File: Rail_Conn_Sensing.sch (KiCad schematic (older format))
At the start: 35 parts, among them U1 AMC1200, U2 AMC1200

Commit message: Upload version 2 files with footprints
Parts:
- removed BT? (x2): 9V, symbol Device:Battery
- removed C? (x2): 100uF, symbol Device:C
- removed D? (x2): Zener, symbol Device:D_Zener
- removed J?: Output, symbol Connector:Screw_Terminal_01x01
- removed R? (x2): 220, symbol Device:R
- added C1, C2, C3, C4: 10uF, symbol Device:C
- added D1, D2: GREEN, symbol Device:LED
- added J3: Outputs, symbol Connector:Screw_Terminal_01x03
- added PS1, PS2: PQMCE1-S5-S5-S, Rail_Conn_Sensing-footprints:CONV_PQMCE1-S5-S5-S, symbol PQMCE1-S5-S5-S:PQMCE1-S5-S5-S
- added R10, R9: 100, Resistor_THT:R_Axial_DIN0207_L6.3mm_D2.5mm_P10.16mm_Horizontal, symbol Device:R
- added unit 4 of U4
- added unit 3 of U4
- R1, R11, R2, R3, R4: renamed from R?; footprint (none) -> Resistor_THT:R_Axial_DIN0207_L6.3mm_D2.5mm_P10.16mm_Horizontal
- R5, R7: renamed from R?; value 10k -> 600; footprint (none) -> Resistor_THT:R_Axial_DIN0207_L6.3mm_D2.5mm_P10.16mm_Horizontal
- R6, R8: renamed from R?; value 1k -> 400; footprint (none) -> Resistor_THT:R_Axial_DIN0207_L6.3mm_D2.5mm_P10.16mm_Horizontal
- U1, U2: footprint (none) -> Rail_Conn_Sensing-footprints:SOIC-8_W7.6mm
- gave numbers to parts that had none: 7
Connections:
- net +3V3 is gone; now on net +5V: U1.8 (VDD2), U2.8 (VDD2)
- net +5V: now also R11.2, U5.5, C4.1, PS1.1 (VIN), PS2.1 (VIN), R10.2, R9.2; no longer R11.1, U5.4
- net GND: now also C3.2, C4.2, PS1.2 (GND), PS2.2 (GND)
- net at J1.2 (Pin_2), R3.2, U1.3 (VINN)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: now also C1.2, PS2.4 (0V)
- net at U1.1 (VDD1): now also C1.1, PS2.6 (+VO)
- net at U2.1 (VDD1): now also C2.1, PS1.6 (+VO)
- net at J1.4 (Pin_4), R4.2, U2.3 (VINN)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: now also C2.2, PS1.4 (0V)
- net at U4.3, U5.1: now also U4.9
- net at U4.6, U5.2: now also U4.13
- net at U5.3: now also U5.4, U4.10, U4.12; no longer U5.5
- net at D3.1 (K), U5.6: now also J3.2 (Pin_2)
- net at D3.2 (A): now also R11.1; no longer R11.2
- net at J2.1 (Pin_1), U6.1 (IN): now also C3.1
- new net: D2.1 (K), J3.3 (Pin_3), U4.11
- new net: D1.1 (K), J3.1 (Pin_1), U4.8
- new net: D1.2 (A), R9.1
- new net: D2.2 (A), R10.1
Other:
- moved on the sheet: D3, J1, J2, R1, R11, R2, R3, R4, R5, R6, R7, R8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

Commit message: Create pcb layout and part assignment
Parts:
- C1, C2, C3, C4: footprint (none) -> Capacitor_THT:C_Radial_D6.3mm_H11.0mm_P2.50mm
- D1, D2, D3: footprint (none) -> LED_THT:LED_D5.0mm
- J1: footprint (none) -> TerminalBlock_Phoenix:TerminalBlock_Phoenix_PT-1,5-4-5.0-H_1x04_P5.00mm_Horizontal
- J2: footprint (none) -> TerminalBlock_Phoenix:TerminalBlock_Phoenix_PT-1,5-2-5.0-H_1x02_P5.00mm_Horizontal
- J3: footprint (none) -> TerminalBlock_Phoenix:TerminalBlock_Phoenix_PT-1,5-3-5.0-H_1x03_P5.00mm_Horizontal
- R1, R10, R11, R2, R3, R4, R5, R6, R7, R8, R9: footprint Resistor_THT:R_Axial_DIN0207_L6.3mm_D2.5mm_P10.16mm_Horizontal -> Resistor_THT:R_Axial_DIN0309_L9.0mm_D3.2mm_P15.24mm_Horizontal
- U3, U4, U5: footprint (none) -> Package_DIP:DIP-14_W7.62mm
- U6: footprint (none) -> Package_TO_SOT_THT:TO-220-3_Horizontal_TabDown

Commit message: Delete extra resistor divider and re-arrange pcb
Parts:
- removed R7: 600, Resistor_THT:R_Axial_DIN0309_L9.0mm_D3.2mm_P15.24mm_Horizontal, symbol Device:R
- removed R8: 400, Resistor_THT:R_Axial_DIN0309_L9.0mm_D3.2mm_P15.24mm_Horizontal, symbol Device:R
- renumbered R9 to R7, R10 to R8, R11 to R9
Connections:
- net at R5.2, R6.1, U3.2 (-)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: now also U3.13 (-), U3.9 (-)
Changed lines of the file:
@@
 Sheet 1 1
 Title "Rail Connection Sensing Circuit"
-Date "2020-06-26"
+Date "2020-06-30"
 Rev "v02"
 Comp ""
@@
 $EndComp
 $Comp
-L power:GND #PWR07
+L power:GND #PWR08
 U 1 1 5EE5082A
 P 4800 3800
-F 0 "#PWR07" H 4800 3550 50  0001 C CNN
+F 0 "#PWR08" H 4800 3550 50  0001 C CNN
 F 1 "GND" H 4805 3627 50  0000 C CNN
 F 2 "" H 4800 3800 50  0001 C CNN
@@
 Wire Wire Line
 	5300 5400 4650 5400
-$Comp
-L Device:R R7
-U 1 1 5EEC90AA
-P 4800 4800
-F 0 "R7" H 4870 4846 50  0000 L CNN
-F 1 "600" H 4870 4755 50  0000 L CNN
-F 2 "Resistor_THT:R_Axial_DIN0309_L9.0mm_D3.2mm_P15.24mm_Horizontal" V 4730 4800 50  0001 C CNN
-F 3 "~" H 4800 4800 50  0001 C CNN
-	1    4800 4800
-	1    0    0    -1
-$EndComp
-$Comp
-L Device:R R8
-U 1 1 5EEC90B0
-P 4800 5200
-F 0 "R8" H 4870 5246 50  0000 L CNN
-F 1 "400" H 4870 5155 50  0000 L CNN
-F 2 "Resistor_THT:R_Axial_DIN0309_L9.0mm_D3.2mm_P15.24mm_Horizontal" V 4730 5200 50  0001 C CNN
-F 3 "~" H 4800 5200 50  0001 C CNN
-	1    4800 5200
-	1    0    0    -1
-$EndComp
 Wire Wire Line
 	4650 5200 4650 5400
@@
 $EndComp
 Wire Wire Line
-	4800 4950 4800 5000
-Wire Wire Line
-	5100 4800 5100 5000
-Wire Wire Line
-	5100 5000 4800 5000
-Connection ~ 4800 5000
-Wire Wire Line
-	4800 5000 4800 5050
-Wire Wire Line
 	5300 5600 5100 5600
 Wire Wire Line
-	5100 5600 5100 5000
-Connection ~ 5100 5000
-Wire Wire Line
 	4450 5200 4650 5200
 Wire Wire Line
 	4450 5300 4550 5300
-Wire Wire Line
-	4550 5300 4550 5500
-Wire Wire Line
-	4800 5350 4800 5500
-Wire Wire Line
-	4550 5500 4800 5500
 $Comp
 L Device:LED D3
@@
 	1    0    0    -1
 $EndComp
-Connection ~ 4800 5500
-$Comp
-L power:GND #PWR08
+$Comp
+L power:GND #PWR03
 U 1 1 5EEC90BD
-P 4800 5550
-F 0 "#PWR08" H 4800 5300 50  0001 C CNN
-F 1 "GND" H 4805 5377 50  0000 C CNN
-F 2 "" H 4800 5550 50  0001 C CNN
-F 3 "" H 4800 5550 50  0001 C CNN
-	1    4800 5550
-	1    0    0    -1
-$EndComp
-Wire Wire Line
-	4800 5500 4800 5550
+P 4550 5550
+F 0 "#PWR03" H 4550 5300 50  0001 C CNN
+F 1 "GND" H 4555 5377 50  0000 C CNN
+F 2 "" H 4550 5550 50  0001 C CNN
+F 3 "" H 4550 5550 50  0001 C CNN
+	1    4550 5550
+	1    0    0    -1
+$EndComp
 Wire Wire Line
 	4800 3500 4800 3800
@@
 	2400 5300 2800 5300
 $Comp
-L Device:R R11
+L Device:R R9
 U 1 1 5F029A20
 P 9200 3650
-F 0 "R11" H 9270 3696 50  0000 L CNN
+F 0 "R9" H 9270 3696 50  0000 L CNN
 F 1 "100" H 9270 3605 50  0000 L CNN
 F 2 "Resistor_THT:R_Axial_DIN0309_L9.0mm_D3.2mm_P15.24mm_Horizontal" V 9130 3650 50  0001 C CNN
@@
 $EndComp
 $Comp
-L power:+5V #PWR05
+L power:+5V #PWR06
 U 1 1 5EEB13E3
 P 4700 1300
-F 0 "#PWR05" H 4700 1150 50  0001 C CNN
+F 0 "#PWR06" H 4700 1150 50  0001 C CNN
 F 1 "+5V" H 4715 1473 50  0000 C CNN
 F 2 "" H 4700 1300 50  0001 C CNN
@@
 	4550 2500 4550 2400
 Wire Wire Line
-	4550 4400 4550 4450
-Wire Wire Line
-	4800 4650 4800 4450
-Wire Wire Line
-	4800 4450 4550 4450
-Connection ~ 4550 4450
-Wire Wire Line
-	4550 4450 4550 5000
-Wire Wire Line
 	3450 3200 3650 3200
 Wire Wire Line
@@
 $EndComp
 $Comp
-L Device:R R10
+L Device:R R8
 U 1 1 5F0A91A6
 P 8600 4650
-F 0 "R10" H 8670 4696 50  0000 L CNN
+F 0 "R8" H 8670 4696 50  0000 L CNN
 F 1 "100" H 8670 4605 50  0000 L CNN
 F 2 "Resistor_THT:R_Axial_DIN0309_L9.0mm_D3.2mm_P15.24mm_Horizontal" V 8530 4650 50  0001 C CNN
@@
 	8800 3550 8750 3550
 $Comp
-L Device:R R9
+L Device:R R7
 U 1 1 5F094ED0
 P 8600 3550
-F 0 "R9" H 8670 3596 50  0000 L CNN
+F 0 "R7" H 8670 3596 50  0000 L CNN
 F 1 "100" H 8670 3505 50  0000 L CNN
 F 2 "Resistor_THT:R_Axial_DIN0309_L9.0mm_D3.2mm_P15.24mm_Horizontal" V 8530 3550 50  0001 C CNN
@@
 	4500 1600 4700 1600
 $Comp
-L power:GND #PWR06
+L power:GND #PWR07
 U 1 1 5EEB771F
 P 4700 1650
-F 0 "#PWR06" H 4700 1400 50  0001 C CNN
+F 0 "#PWR07" H 4700 1400 50  0001 C CNN
 F 1 "GND" H 4705 1477 50  0000 C CNN
 F 2 "" H 4700 1650 50  0001 C CNN
@@
 	4500 1400 4700 1400
 $Comp
-L power:+5V #PWR03
+L power:+5V #PWR04
 U 1 1 5F386CEF
 P 4650 6200
-F 0 "#PWR03" H 4650 6050 50  0001 C CNN
+F 0 "#PWR04" H 4650 6050 50  0001 C CNN
 F 1 "+5V" H 4665 6373 50  0000 C CNN
 F 2 "" H 4650 6200 50  0001 C CNN
@@
 	4450 6500 4650 6500
 $Comp
-L power:GND #PWR04
+L power:GND #PWR05
 U 1 1 5F386CF7
 P 4650 6550
-F 0 "#PWR04" H 4650 6300 50  0001 C CNN
+F 0 "#PWR05" H 4650 6300 50  0001 C CNN
 F 1 "GND" H 4655 6377 50  0000 C CNN
 F 2 "" H 4650 6550 50  0001 C CNN
@@
 	2100 6200 2100 4850
 Connection ~ 3250 6200
+Wire Wire Line
+	4550 4400 4550 5000
+Wire Wire Line
+	5100 4800 5100 5600
+Wire Wire Line
+	4550 5300 4550 5550
+Wire Wire Line
+	5100 4800 5100 3600
+Connection ~ 5100 4800
+Connection ~ 5100 3600
 $EndSCHEMATC

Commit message: Fix up wires and move silk screen labels
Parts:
- C1, C2, C3, C4: footprint Capacitor_THT:C_Radial_D6.3mm_H11.0mm_P2.50mm -> Capacitor_THT:CP_Radial_D6.3mm_P2.50mm; symbol Device:C -> Device:CP1
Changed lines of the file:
@@
 	4450 6300 4650 6300
 $Comp
-L Device:C C1
+L Device:CP1 C1
 U 1 1 5EF2E610
 P 3150 1550
 F 0 "C1" H 3265 1596 50  0000 L CNN
 F 1 "10uF" H 3265 1505 50  0000 L CNN
-F 2 "Capacitor_THT:C_Radial_D6.3mm_H11.0mm_P2.50mm" H 3188 1400 50  0001 C CNN
+F 2 "Capacitor_THT:CP_Radial_D6.3mm_P2.50mm" H 3188 1400 50  0001 C CNN
 F 3 "~" H 3150 1550 50  0001 C CNN
 	1    3150 1550
@@
 	2050 1700 2050 3450
 $Comp
-L Device:C C3
+L Device:CP1 C3
 U 1 1 5EF511EA
 P 7050 1750
 F 0 "C3" H 7165 1796 50  0000 L CNN
 F 1 "10uF" H 7165 1705 50  0000 L CNN
-F 2 "Capacitor_THT:C_Radial_D6.3mm_H11.0mm_P2.50mm" H 7088 1600 50  0001 C CNN
+F 2 "Capacitor_THT:CP_Radial_D6.3mm_P2.50mm" H 7088 1600 50  0001 C CNN
 F 3 "~" H 7050 1750 50  0001 C CNN
 	1    7050 1750
@@
 	6950 1600 7050 1600
 $Comp
-L Device:C C2
+L Device:CP1 C2
 U 1 1 5EF72AA8
 P 3250 6350
 F 0 "C2" H 3365 6396 50  0000 L CNN
 F 1 "10uF" H 3365 6305 50  0000 L CNN
-F 2 "Capacitor_THT:C_Radial_D6.3mm_H11.0mm_P2.50mm" H 3288 6200 50  0001 C CNN
+F 2 "Capacitor_THT:CP_Radial_D6.3mm_P2.50mm" H 3288 6200 50  0001 C CNN
 F 3 "~" H 3250 6350 50  0001 C CNN
 	1    3250 6350
@@
 $EndComp
 $Comp
-L Device:C C4
+L Device:CP1 C4
 U 1 1 5EF7AB8D
 P 10700 1750
 F 0 "C4" H 10815 1796 50  0000 L CNN
 F 1 "10uF" H 10815 1705 50  0000 L CNN
-F 2 "Capacitor_THT:C_Radial_D6.3mm_H11.0mm_P2.50mm" H 10738 1600 50  0001 C CNN
+F 2 "Capacitor_THT:CP_Radial_D6.3mm_P2.50mm" H 10738 1600 50  0001 C CNN
 F 3 "~" H 10700 1750 50  0001 C CNN
 	1    10700 1750

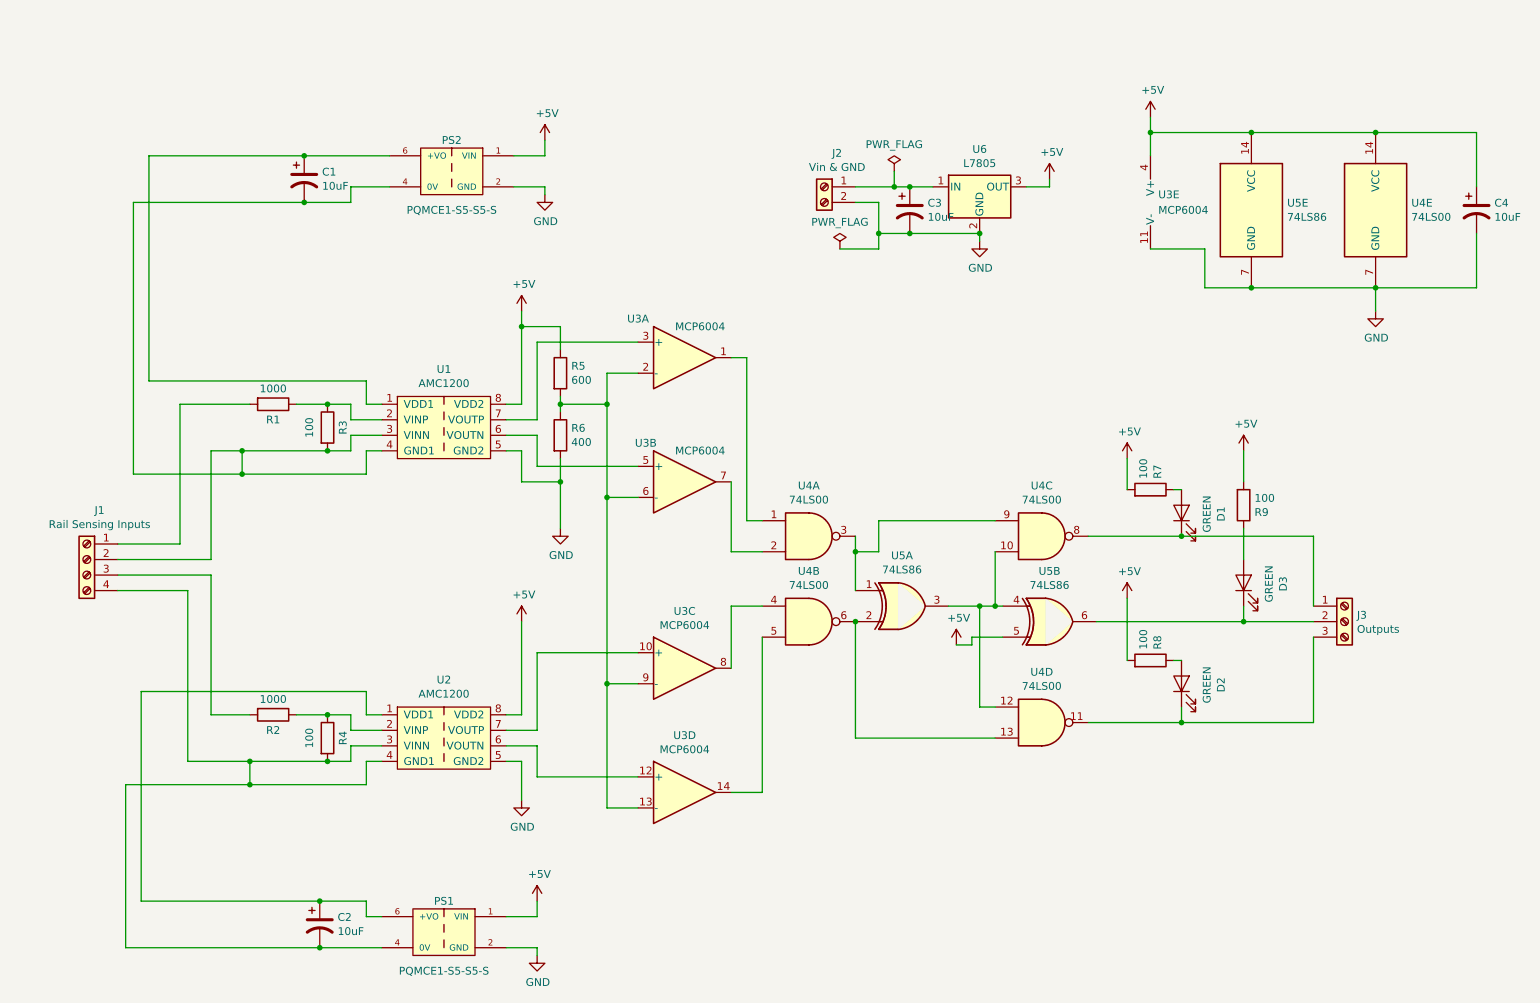
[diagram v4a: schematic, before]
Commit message: Add connections to ground for floating unused input pins
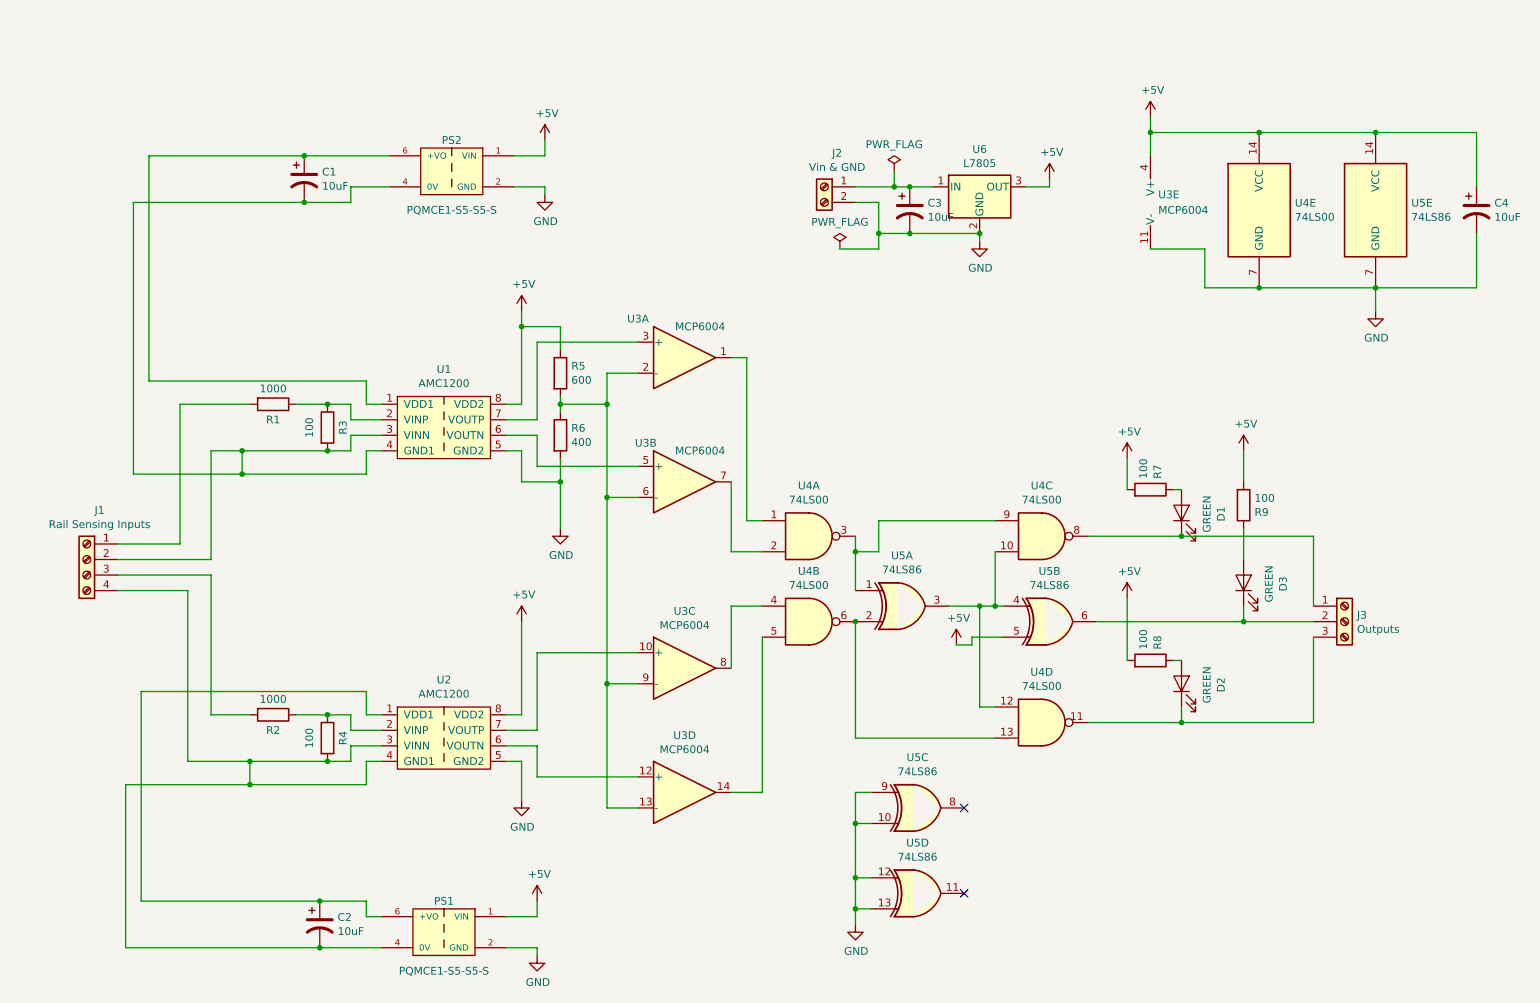
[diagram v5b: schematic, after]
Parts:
- added unit 3 of U5
- added unit 4 of U5
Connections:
- net GND: now also U5.10, U5.12, U5.13, U5.9
- no-connect marks 0 -> 2
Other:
- moved on the sheet: U4E
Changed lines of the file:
@@
 Sheet 1 1
 Title "Rail Connection Sensing Circuit"
-Date "2020-06-30"
+Date "2020-07-06"
 Rev "v02"
 Comp ""
@@
 $EndComp
 $Comp
-L 74xx:74LS86 U5
-U 5 1 5EF05567
-P 9250 1750
-F 0 "U5" H 9480 1796 50  0000 L CNN
-F 1 "74LS86" H 9480 1705 50  0000 L CNN
-F 2 "Package_DIP:DIP-14_W7.62mm" H 9250 1750 50  0001 C CNN
-F 3 "74xx/74ls86.pdf" H 9250 1750 50  0001 C CNN
-	5    9250 1750
-	1    0    0    -1
-$EndComp
-$Comp
 L 74xx:74LS00 U4
 U 5 1 5EF071CD
-P 10050 1750
-F 0 "U4" H 10280 1796 50  0000 L CNN
-F 1 "74LS00" H 10280 1705 50  0000 L CNN
-F 2 "Package_DIP:DIP-14_W7.62mm" H 10050 1750 50  0001 C CNN
-F 3 "http://www.ti.com/lit/gpn/sn74ls00" H 10050 1750 50  0001 C CNN
-	5    10050 1750
+P 9300 1750
+F 0 "U4" H 9530 1796 50  0000 L CNN
+F 1 "74LS00" H 9530 1705 50  0000 L CNN
+F 2 "Package_DIP:DIP-14_W7.62mm" H 9300 1750 50  0001 C CNN
+F 3 "http://www.ti.com/lit/gpn/sn74ls00" H 9300 1750 50  0001 C CNN
+	5    9300 1750
 	1    0    0    -1
 $EndComp
@@
 Wire Wire Line
 	8600 1250 8600 1400
-Wire Wire Line
-	8600 1250 9250 1250
 $Comp
 L power:GND #PWR016
@@
 Wire Wire Line
 	10050 2250 10050 2400
-Wire Wire Line
-	9250 2250 10050 2250
 Connection ~ 10050 2250
 Wire Wire Line
 	8950 2000 8950 2250
 Wire Wire Line
-	8950 2250 9250 2250
-Connection ~ 9250 2250
-Wire Wire Line
 	8600 2000 8950 2000
 Wire Wire Line
 	8600 1150 8600 1250
-Wire Wire Line
-	10050 1250 9250 1250
-Connection ~ 9250 1250
 $Comp
 L Connector:Screw_Terminal_01x04 J1
@@
 	10700 1600 10700 1250
 Wire Wire Line
-	10700 1250 10050 1250
-Connection ~ 10050 1250
-Wire Wire Line
 	10700 1900 10700 2250
 Wire Wire Line
@@
 Connection ~ 5100 4800
 Connection ~ 5100 3600
+$Comp
+L 74xx:74LS86 U5
+U 3 1 5F0480D1
+P 7100 5600
+F 0 "U5" H 7100 5925 50  0000 C CNN
+F 1 "74LS86" H 7100 5834 50  0000 C CNN
+F 2 "Package_DIP:DIP-14_W7.62mm" H 7100 5600 50  0001 C CNN
+F 3 "74xx/74ls86.pdf" H 7100 5600 50  0001 C CNN
+	3    7100 5600
+	1    0    0    -1
+$EndComp
+$Comp
+L 74xx:74LS86 U5
+U 4 1 5F051C11
+P 7100 6150
+F 0 "U5" H 7100 6475 50  0000 C CNN
+F 1 "74LS86" H 7100 6384 50  0000 C CNN
+F 2 "Package_DIP:DIP-14_W7.62mm" H 7100 6150 50  0001 C CNN
+F 3 "74xx/74ls86.pdf" H 7100 6150 50  0001 C CNN
+	4    7100 6150
+	1    0    0    -1
+$EndComp
+$Comp
+L power:GND #PWR017
+U 1 1 5F06CCD5
+P 6700 6350
+F 0 "#PWR017" H 6700 6100 50  0001 C CNN
+F 1 "GND" H 6705 6177 50  0000 C CNN
+F 2 "" H 6700 6350 50  0001 C CNN
+F 3 "" H 6700 6350 50  0001 C CNN
+	1    6700 6350
+	1    0    0    -1
+$EndComp
+Wire Wire Line
+	6800 6250 6700 6250
+Wire Wire Line
+	6700 6250 6700 6350
+Wire Wire Line
+	6800 6050 6700 6050
+Wire Wire Line
+	6700 6050 6700 6250
+Connection ~ 6700 6250
+Wire Wire Line
+	6800 5700 6700 5700
+Wire Wire Line
+	6700 5700 6700 6050
+Connection ~ 6700 6050
+Wire Wire Line
+	6800 5500 6700 5500
+Wire Wire Line
+	6700 5500 6700 5700
+Connection ~ 6700 5700
+NoConn ~ 7400 5600
+NoConn ~ 7400 6150
+Wire Wire Line
+	8600 1250 9300 1250
+Wire Wire Line
+	8950 2250 9300 2250
+$Comp
+L 74xx:74LS86 U5
+U 5 1 5F0EC34F
+P 10050 1750
+F 0 "U5" H 10280 1796 50  0000 L CNN
+F 1 "74LS86" H 10280 1705 50  0000 L CNN
+F 2 "Package_DIP:DIP-14_W7.62mm" H 10050 1750 50  0001 C CNN
+F 3 "74xx/74ls86.pdf" H 10050 1750 50  0001 C CNN
+	5    10050 1750
+	1    0    0    -1
+$EndComp
+Connection ~ 9300 1250
+Connection ~ 9300 2250
+Wire Wire Line
+	9300 2250 10050 2250
+Wire Wire Line
+	9300 1250 10050 1250
+Connection ~ 10050 1250
+Wire Wire Line
+	10050 1250 10700 1250
 $EndSCHEMATC
